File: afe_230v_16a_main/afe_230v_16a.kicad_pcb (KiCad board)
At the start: 2 copper layers, 146 x 86.4 mm, 68 parts, among them J1 MKDSN 2,5/ 6-5,08, J2 MKDS 1,5/ 6, J5 HBUS16, J6 pinheader_2x6_socket, J9 Conn_01x04_STlink_pinheader, U10 BlackPill_F4_SWI, U2 AD8538, U3 AD8538_dnp, U4 AQH3223A, U5 ACS711xLCTR-25AB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

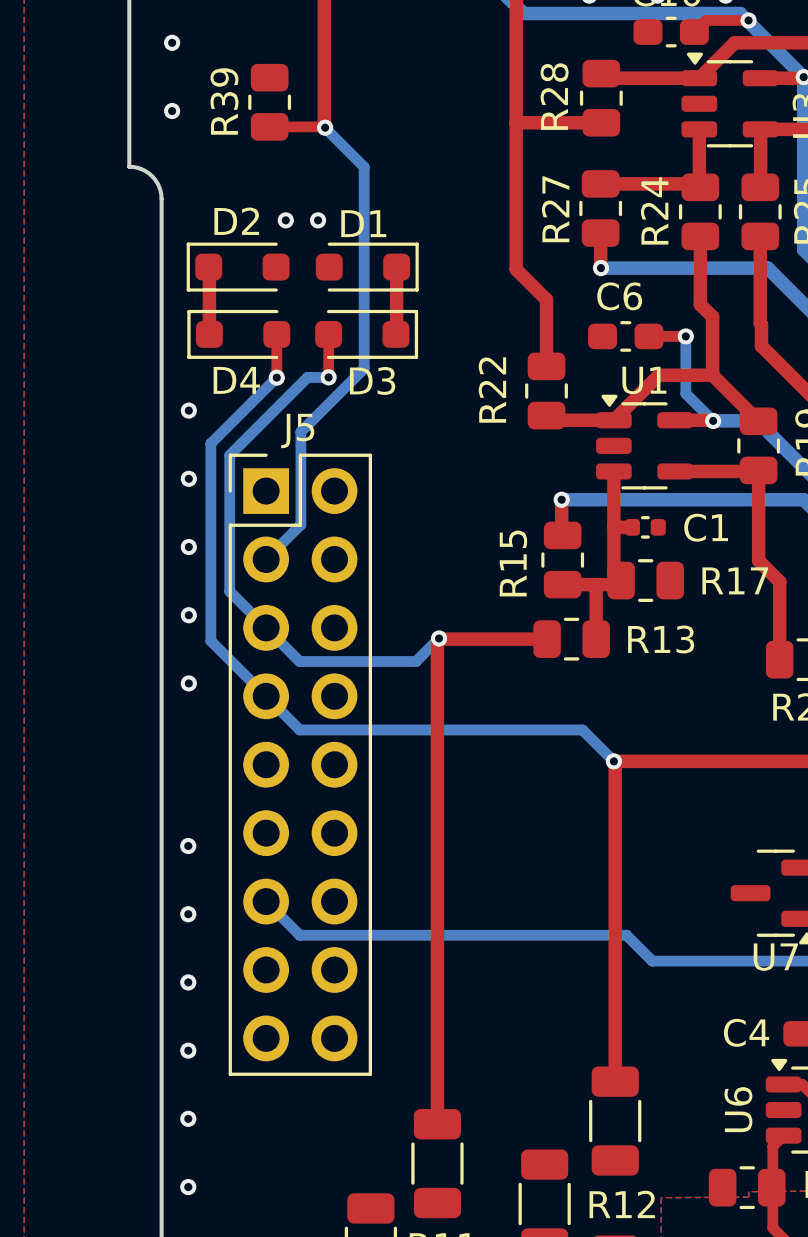
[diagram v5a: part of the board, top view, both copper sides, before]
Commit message: fixed hbus location, added bc71,6 edgecuts'
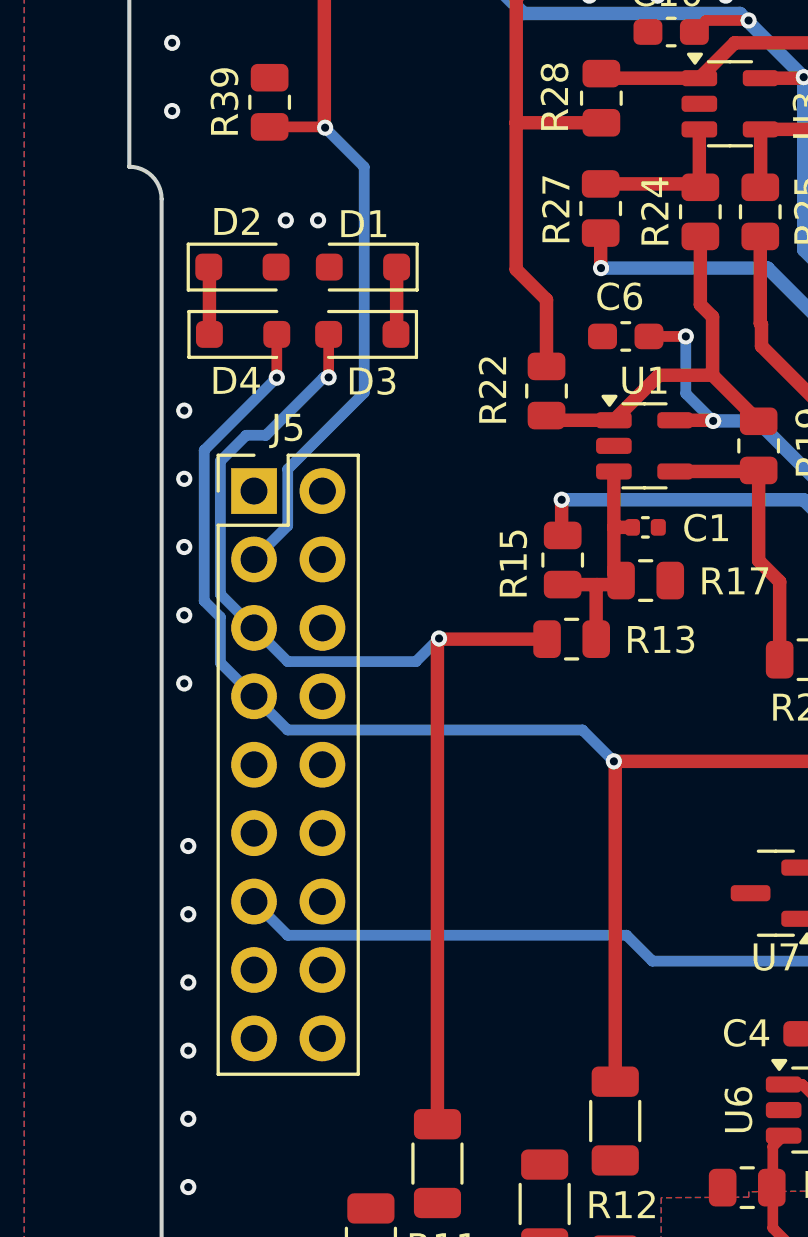
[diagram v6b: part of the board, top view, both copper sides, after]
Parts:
- moved J5 0.45 mm to (122.6, 84.5)
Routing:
- net /V0_sense: track 42.8 -> 43.4 mm
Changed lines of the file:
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@@
 		(tags "resistor")
 		(property "Reference" "R32"
-			(at -3.38 0.08 360)
+			(at -3.38 0.08 0)
 			(layer "F.SilkS")
 			(effects
@@
 		)
 		(property "Value" "1KR"
-			(at 0 1.65 360)
+			(at 0 1.65 0)
 			(layer "F.Fab")
 			(effects
@@
 		)
 		(fp_text user "${REFERENCE}"
-			(at 0 0 360)
+			(at 0 0 0)
 			(layer "F.Fab")
 			(effects
@@
 		(locked yes)
 		(layer "F.Cu")
-		(at 123.03 84.49)
+		(at 122.58 84.49)
 		(descr "Through hole straight pin header, 2x09, 2.54mm pitch, double rows")
 		(tags "Through hole pin header THT 2x09 2.54mm double row")
@@
 	)
 	(gr_line
+		(start 118.7 73.65)
+		(end 118.7 115.65)
+		(stroke
+			(width 0.05)
+			(type default)
+		)
+		(layer "User.3")
+	)
+	(gr_line
 		(start 245.52 99.31)
 		(end 245.52 86.31)
@@
 	)
 	(gr_line
+		(start 118.7 94.65)
+		(end 122.58 94.65)
+		(stroke
+			(width 0.1)
+			(type default)
+		)
+		(layer "User.3")
+	)
+	(gr_line
+		(start 119.15 73.65)
+		(end 118.7 73.65)
+		(stroke
+			(width 0.05)
+			(type default)
+		)
+		(layer "User.3")
+	)
+	(gr_line
 		(start 151.8 63.35)
 		(end 151.8 125.95)
@@
 	)
 	(gr_line
+		(start 119.15 115.65)
+		(end 118.7 115.65)
+		(stroke
+			(width 0.05)
+			(type default)
+		)
+		(layer "User.3")
+	)
+	(gr_line
 		(start 262.7 99.31)
 		(end 245.52 99.31)
@@
 	)
 	(via
-		(at 120.16 91.632148)
+		(at 119.99 91.632148)
 		(size 0.6)
 		(drill 0.3)
@@
 	)
 	(via
-		(at 120.16 84.035716)
+		(at 119.99 84.035716)
 		(size 0.6)
 		(drill 0.3)
@@
 	)
 	(via
-		(at 120.16 81.503574)
+		(at 119.99 81.503574)
 		(size 0.6)
 		(drill 0.3)
@@
 	)
 	(via
-		(at 120.16 89.1)
+		(at 119.99 89.1)
 		(size 0.6)
 		(drill 0.3)
@@
 	)
 	(via
-		(at 120.16 86.567858)
+		(at 119.99 86.567858)
 		(size 0.6)
 		(drill 0.3)
@@
 	)
 	(segment
-		(start 121.68 83.16)
-		(end 121.68 88.22)
+		(start 123.83 90.82)
+		(end 122.58 89.57)
 		(width 0.4)
 		(layer "B.Cu")
@@
 	)
 	(segment
-		(start 128.5925 90.82)
-		(end 124.28 90.82)
+		(start 121.33 83.38)
+		(end 122.29 82.42)
 		(width 0.4)
 		(layer "B.Cu")
@@
 	)
 	(segment
-		(start 121.68 88.22)
-		(end 123.03 89.57)
+		(start 121.33 88.32)
+		(end 121.33 83.38)
 		(width 0.4)
 		(layer "B.Cu")
@@
 	)
 	(segment
-		(start 124.57 80.27)
-		(end 121.68 83.16)
+		(start 123.02 82.42)
+		(end 125.17 80.27)
 		(width 0.4)
 		(layer "B.Cu")
@@
 	)
 	(segment
-		(start 125.35 80.27)
-		(end 124.57 80.27)
+		(start 122.29 82.42)
+		(end 123.02 82.42)
 		(width 0.4)
 		(layer "B.Cu")
@@
 	)
 	(segment
-		(start 124.28 90.82)
-		(end 123.03 89.57)
+		(start 122.58 89.57)
+		(end 121.33 88.32)
+		(width 0.4)
+		(layer "B.Cu")
+		(net 6)
+	)
+	(segment
+		(start 128.5925 90.82)
+		(end 123.83 90.82)
+		(width 0.4)
+		(layer "B.Cu")
+		(net 6)
+	)
+	(segment
+		(start 125.17 80.27)
+		(end 125.35 80.27)
 		(width 0.4)
 		(layer "B.Cu")
@@
 	)
 	(segment
-		(start 123.03 92.11)
-		(end 124.28 93.36)
+		(start 135.94 94.525)
+		(end 134.775 93.36)
 		(width 0.4)
 		(layer "B.Cu")
@@
 	)
 	(segment
-		(start 120.98 82.725)
-		(end 120.98 90.06)
+		(start 121.33 89.168528)
+		(end 120.73 88.568528)
 		(width 0.4)
 		(layer "B.Cu")
@@
 	)
 	(segment
-		(start 124.28 93.36)
-		(end 134.775 93.36)
+		(start 122.58 92.11)
+		(end 121.33 90.86)
 		(width 0.4)
 		(layer "B.Cu")
@@
 	)
 	(segment
-		(start 134.775 93.36)
-		(end 135.94 94.525)
+		(start 123.83 93.36)
+		(end 122.58 92.11)
 		(width 0.4)
 		(layer "B.Cu")
@@
 	)
 	(segment
-		(start 123.425 80.28)
-		(end 120.98 82.725)
+		(start 120.73 88.568528)
+		(end 120.73 82.975)
 		(width 0.4)
 		(layer "B.Cu")
@@
 	)
 	(segment
-		(start 120.98 90.06)
-		(end 123.03 92.11)
+		(start 120.73 82.975)
+		(end 123.425 80.28)
+		(width 0.4)
+		(layer "B.Cu")
+		(net 7)
+	)
+	(segment
+		(start 121.33 90.86)
+		(end 121.33 89.168528)
+		(width 0.4)
+		(layer "B.Cu")
+		(net 7)
+	)
+	(segment
+		(start 134.775 93.36)
+		(end 123.83 93.36)
 		(width 0.4)
 		(layer "B.Cu")
@@
 	)
 	(segment
-		(start 124.32 85.74)
-		(end 124.32 82.28995)
-		(width 0.4)
-		(layer "B.Cu")
-		(net 15)
-	)
-	(segment
 		(start 166.71 57.385)
 		(end 168 58.675)
@@
 	)
 	(segment
-		(start 126.67 79.93995)
-		(end 126.67 72.46)
+		(start 125.22 71.01)
+		(end 125.22 71)
 		(width 0.4)
 		(layer "B.Cu")
@@
 	)
 	(segment
-		(start 126.67 72.46)
-		(end 125.22 71.01)
+		(start 126.67 80.84)
+		(end 126.67 72.46)
 		(width 0.4)
 		(layer "B.Cu")
@@
 	)
 	(segment
-		(start 169.02 82.9)
-		(end 171.56 82.9)
+		(start 122.58 87.03)
+		(end 123.83 85.78)
 		(width 0.4)
 		(layer "B.Cu")
@@
 	)
 	(segment
-		(start 123.03 87.03)
-		(end 124.32 85.74)
+		(start 169.02 82.9)
+		(end 171.56 82.9)
 		(width 0.4)
 		(layer "B.Cu")
@@
 	)
 	(segment
-		(start 125.22 71.01)
-		(end 125.22 71)
+		(start 126.67 72.46)
+		(end 125.22 71.01)
 		(width 0.4)
 		(layer "B.Cu")
@@
 	)
 	(segment
-		(start 124.32 82.28995)
-		(end 126.67 79.93995)
+		(start 123.83 83.68)
+		(end 126.67 80.84)
 		(width 0.4)
 		(layer "B.Cu")
@@
 	)
 	(segment
+		(start 123.83 85.78)
+		(end 123.83 83.68)
+		(width 0.4)
+		(layer "B.Cu")
+		(net 15)
+	)
+	(segment
 		(start 135.475 70.8175)
 		(end 132.315 70.8175)
@@
 	)
 	(segment
-		(start 136.41 100.98)
-		(end 124.28 100.98)
+		(start 137.37 101.94)
+		(end 136.41 100.98)
 		(width 0.4)
 		(layer "B.Cu")
@@
 	)
 	(segment
-		(start 151.035 101.94)
-		(end 137.37 101.94)
+		(start 123.83 100.98)
+		(end 122.58 99.73)
 		(width 0.4)
 		(layer "B.Cu")
@@
 	)
 	(segment
-		(start 137.37 101.94)
-		(end 136.41 100.98)
+		(start 152.875 100.1)
+		(end 151.035 101.94)
 		(width 0.4)
 		(layer "B.Cu")
@@
 	)
 	(segment
-		(start 124.28 100.98)
-		(end 123.03 99.73)
+		(start 136.41 100.98)
+		(end 123.83 100.98)
 		(width 0.4)
 		(layer "B.Cu")
@@
 	)
 	(segment
-		(start 152.875 100.1)
-		(end 151.035 101.94)
+		(start 151.035 101.94)
+		(end 137.37 101.94)
 		(width 0.4)
 		(layer "B.Cu")
@@
 		(polygon
 			(pts
-				(xy 184.45 95.95) (xy 182.75 95.95) (xy 182.75 93.625) (xy 184.45 93.625)
+				(xy 184.45 95.95) (xy 183.48 95.95) (xy 183.48 93.625) (xy 184.45 93.625)
 			)
 		)
@@
 		(polygon
 			(pts
-				(xy 120.85 95.925) (xy 119.15 95.925) (xy 119.15 93.6) (xy 120.85 93.6)
+				(xy 119.67 95.835) (xy 118.7 95.835) (xy 118.7 93.51) (xy 119.67 93.51)
 			)
 		)

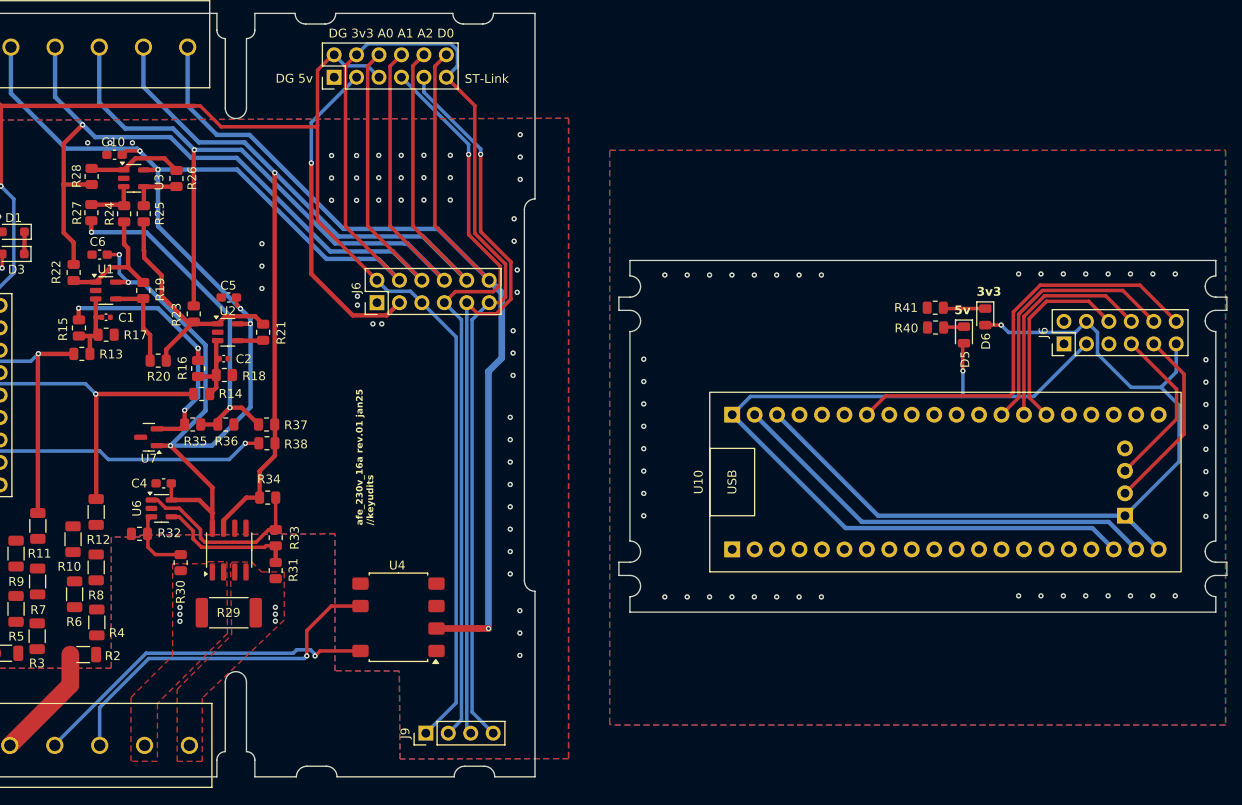
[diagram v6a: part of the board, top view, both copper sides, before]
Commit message: adjusted inter-pcb-connector location, added edgecuts pcb2,3,4,8,9
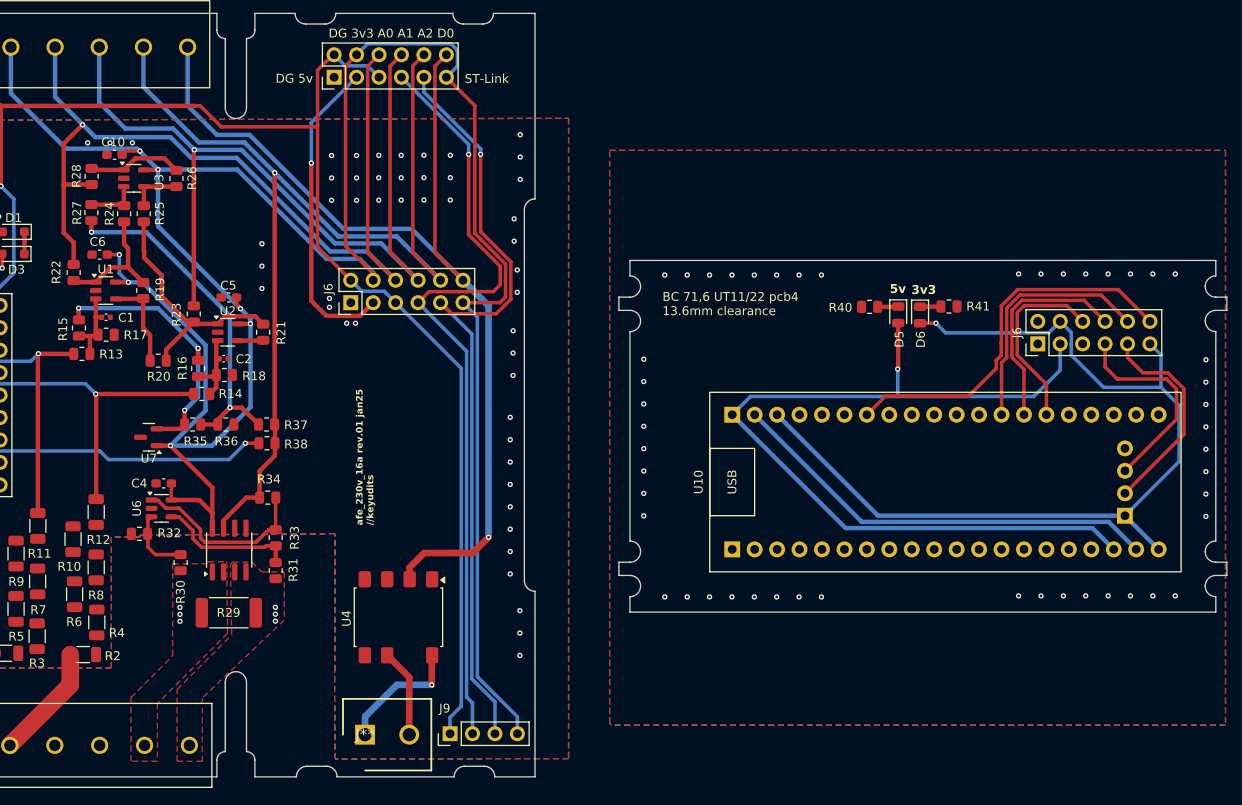
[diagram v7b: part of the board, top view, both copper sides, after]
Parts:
- added J**: SHDR2W130P0X500_1X2_1000X810X1000P, kyuditsky:1985849_SHDR2W130P0X500_1X2_1000X810X1000P, F.Cu at (166.4, 133.1)
- moved R40 7.83 mm to (223.5, 84.7)
- moved D5 7.78 mm to (226.8, 85.6)
- moved D6 7.38 mm to (229.2, 85.6)
- moved J6 2.97 mm to (164.8, 84.2)
- moved J6 2.97 mm to (242.6, 88.8)
- moved J9 2.74 mm to (176.0, 133.0)
- moved R41 1.56 mm to (232.5, 84.6), turned to 180 degrees
- turned U4 to -90 degrees
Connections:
- J1 pad 3: /K_i -> (no net)
- J1 pad 4: /K_o -> (no net)
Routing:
- net /K_o: track 40.3 -> 10.0 mm, vias 1 -> 0
- net /K_i: track 40.1 -> 14.5 mm
- net /D0: track 172.2 -> 158.5 mm
- net /DIO: track 105.4 -> 114.3 mm
- net /SCK: track 104.3 -> 113.0 mm
- net /3V3: track 380.8 -> 388.3 mm
- net /A2: track 152.4 -> 146.0 mm
- net /A1: track 125.4 -> 120.1 mm
- net /A0: track 127.1 -> 121.9 mm
- net Net-(D6-K): track 4.79 -> 2.37 mm
- net /DGND: track 168.2 -> 167.6 mm
